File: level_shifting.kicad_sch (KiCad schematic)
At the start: 22 parts, among them J48 Conn_02x08_Odd_Even, J49 Conn_01x04, J50 Conn_02x08_Odd_Even, U25 TXS0108EPW

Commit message: WIP v0.2.0 changes
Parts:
- removed J48, J50: Conn_02x08_Odd_Even, HL_Connector_Pad_2.54mm:Pad_2x08_P2.54_1.7x1.7_Rect-Oct, symbol Connector_Generic:Conn_02x08_Odd_Even
- removed J49: Conn_01x04, HL_Connector_Pad_2.54mm:Pad_1x04_P2.54_1.7x1.7_Rect-Rnd-Rnd-Rect, symbol Connector_Generic:Conn_01x04
- added J106: Conn_01x04, HL_Connector_Pad_2.54mm:Pad_1x04_P2.54_1.7x1.7_Rect, symbol Connector_Generic:Conn_01x04
- added J80, J85: Conn_01x08, HL_Connector_Pad_2.54mm:Pad_1x08_P2.54_1.7x1.7_Oct, symbol Connector_Generic:Conn_01x08
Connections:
- net Ac1: now also J85.1 (Pin_1)
- net Ac2: now also J85.2 (Pin_2)
- net Ac3: now also J85.3 (Pin_3)
- net Ac4: now also J85.4 (Pin_4)
- net Ac5: now also J85.5 (Pin_5)
- net Ac6: now also J85.6 (Pin_6)
- net Ac7: now also J85.7 (Pin_7)
- net Ac8: now also J85.8 (Pin_8)
- net Bc1: now also J80.1 (Pin_1)
- net Bc2: now also J80.2 (Pin_2)
- net Bc3: now also J80.3 (Pin_3)
- net Bc4: now also J80.4 (Pin_4)
- net Bc5: now also J80.5 (Pin_5)
- net Bc6: now also J80.6 (Pin_6)
- net Bc7: now also J80.7 (Pin_7)
- net Bc8: now also J80.8 (Pin_8)
- net GND: now also J106.1 (Pin_1), J106.2 (Pin_2), J106.3 (Pin_3), J106.4 (Pin_4)
- net VCCA renamed +3.3V
- net VCCB renamed +5V

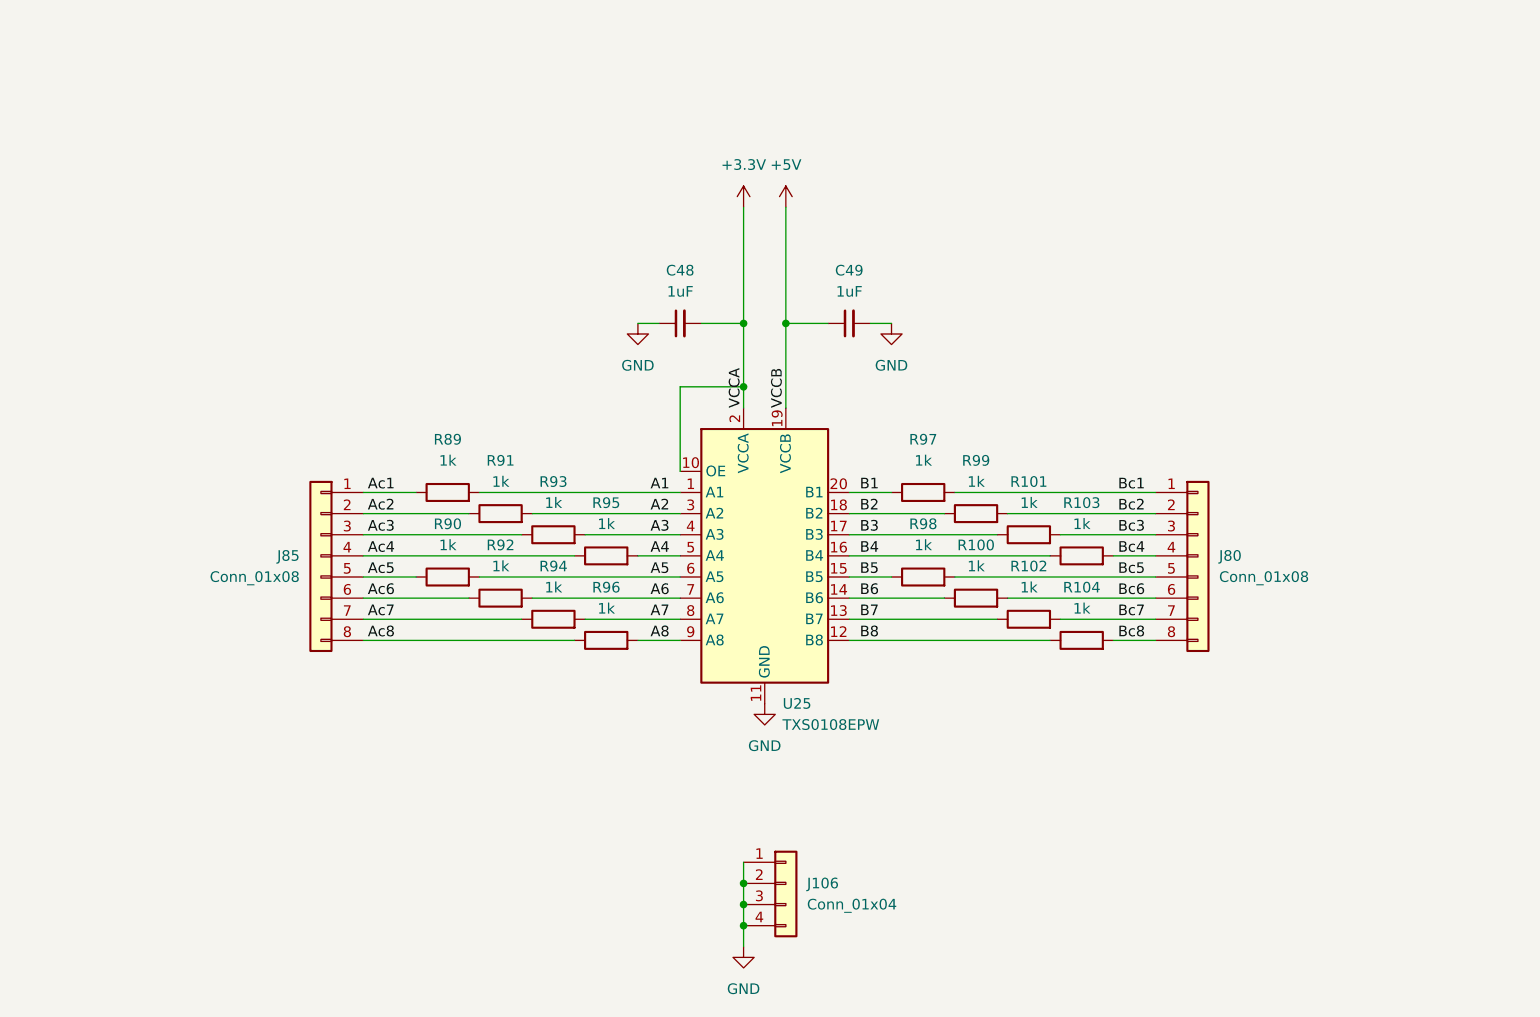
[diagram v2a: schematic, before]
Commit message: Assign part numbers and finish other 0.2.0 changes
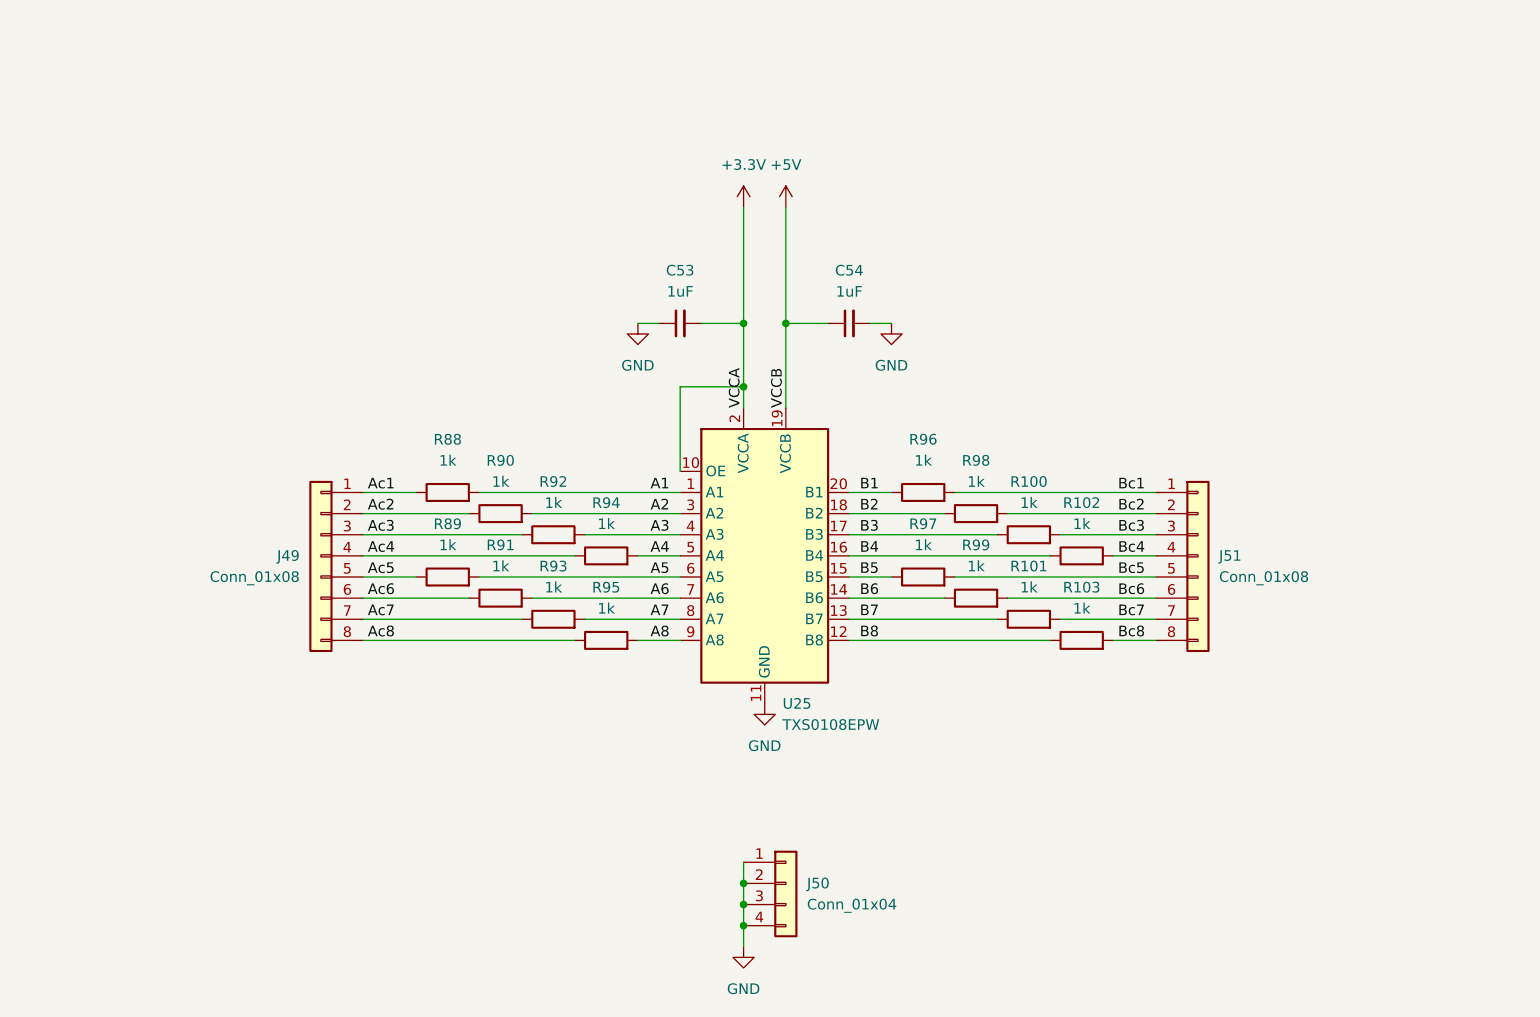
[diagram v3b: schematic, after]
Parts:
- J49: renamed from J85; LCSC (none) -> C492407
- J50: renamed from J106; LCSC (none) -> C2691448
- J51: renamed from J80; LCSC (none) -> C492407
- renumbered C48 to C53, C49 to C54, R101 to R100, R102 to R101, R103 to R102, R104 to R103, R89 to R88, R90 to R89, R91 to R90, R92 to R91, R93 to R92, R94 to R93, R95 to R94, R96 to R95, R97 to R96, R98 to R97, R99 to R98, R100 to R99
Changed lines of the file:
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@@
 		(dnp no)
 		(fields_autoplaced yes)
-		(property "Reference" "#PWR0280"
+		(property "Reference" "#PWR0205"
 			(at 135.89 46.99 0)
 			(effects
@@
 			(project "HALSPA"
 				(path "/7eeba806-440e-4671-bc07-69fe183910a7/47d24875-8df4-4f2a-9eb7-424cf9f25e0d"
-					(reference "#PWR0280")
+					(reference "#PWR0205")
 					(unit 1)
 				)
@@
 		(dnp no)
 		(fields_autoplaced yes)
-		(property "Reference" "C48"
+		(property "Reference" "C53"
 			(at 123.1963 50.8 90)
 			(effects
@@
 			(project ""
 				(path "/7eeba806-440e-4671-bc07-69fe183910a7/47d24875-8df4-4f2a-9eb7-424cf9f25e0d"
-					(reference "C48")
+					(reference "C53")
 					(unit 1)
 				)
@@
 		(dnp no)
 		(fields_autoplaced yes)
-		(property "Reference" "R95"
+		(property "Reference" "R94"
 			(at 114.3 78.74 90)
 			(effects
@@
 			(project "HALSPA"
 				(path "/7eeba806-440e-4671-bc07-69fe183910a7/47d24875-8df4-4f2a-9eb7-424cf9f25e0d"
-					(reference "R95")
+					(reference "R94")
 					(unit 1)
 				)
@@
 		(dnp no)
 		(fields_autoplaced yes)
-		(property "Reference" "C49"
+		(property "Reference" "C54"
 			(at 143.5163 50.8 90)
 			(effects
@@
 			(project "HALSPA"
 				(path "/7eeba806-440e-4671-bc07-69fe183910a7/47d24875-8df4-4f2a-9eb7-424cf9f25e0d"
-					(reference "C49")
+					(reference "C54")
 					(unit 1)
 				)
@@
 		(dnp no)
 		(fields_autoplaced yes)
-		(property "Reference" "R93"
+		(property "Reference" "R92"
 			(at 107.95 76.2 90)
 			(effects
@@
 			(project "HALSPA"
 				(path "/7eeba806-440e-4671-bc07-69fe183910a7/47d24875-8df4-4f2a-9eb7-424cf9f25e0d"
-					(reference "R93")
+					(reference "R92")
 					(unit 1)
 				)
@@
 		(dnp no)
 		(fields_autoplaced yes)
-		(property "Reference" "R92"
+		(property "Reference" "R91"
 			(at 101.6 83.82 90)
 			(effects
@@
 			(project "HALSPA"
 				(path "/7eeba806-440e-4671-bc07-69fe183910a7/47d24875-8df4-4f2a-9eb7-424cf9f25e0d"
-					(reference "R92")
+					(reference "R91")
 					(unit 1)
 				)
@@
 		(dnp no)
 		(fields_autoplaced yes)
-		(property "Reference" "R94"
+		(property "Reference" "R93"
 			(at 107.95 86.36 90)
 			(effects
@@
 			(project "HALSPA"
 				(path "/7eeba806-440e-4671-bc07-69fe183910a7/47d24875-8df4-4f2a-9eb7-424cf9f25e0d"
-					(reference "R94")
+					(reference "R93")
 					(unit 1)
 				)
@@
 		(dnp no)
 		(fields_autoplaced yes)
-		(property "Reference" "#PWR0194"
+		(property "Reference" "#PWR0206"
 			(at 148.59 63.5 0)
 			(effects
@@
 			(project "HALSPA"
 				(path "/7eeba806-440e-4671-bc07-69fe183910a7/47d24875-8df4-4f2a-9eb7-424cf9f25e0d"
-					(reference "#PWR0194")
+					(reference "#PWR0206")
 					(unit 1)
 				)
@@
 		(dnp no)
 		(fields_autoplaced yes)
-		(property "Reference" "R91"
+		(property "Reference" "R90"
 			(at 101.6 73.66 90)
 			(effects
@@
 			(project "HALSPA"
 				(path "/7eeba806-440e-4671-bc07-69fe183910a7/47d24875-8df4-4f2a-9eb7-424cf9f25e0d"
-					(reference "R91")
+					(reference "R90")
 					(unit 1)
 				)
@@
 		(dnp no)
 		(fields_autoplaced yes)
-		(property "Reference" "R104"
+		(property "Reference" "R103"
 			(at 171.45 88.9 90)
 			(effects
@@
 			(project "HALSPA"
 				(path "/7eeba806-440e-4671-bc07-69fe183910a7/47d24875-8df4-4f2a-9eb7-424cf9f25e0d"
-					(reference "R104")
+					(reference "R103")
 					(unit 1)
 				)
@@
 		(dnp no)
 		(fields_autoplaced yes)
-		(property "Reference" "R101"
+		(property "Reference" "R100"
 			(at 165.1 76.2 90)
 			(effects
@@
 			(project "HALSPA"
 				(path "/7eeba806-440e-4671-bc07-69fe183910a7/47d24875-8df4-4f2a-9eb7-424cf9f25e0d"
-					(reference "R101")
+					(reference "R100")
 					(unit 1)
 				)
@@
 		(dnp no)
 		(fields_autoplaced yes)
-		(property "Reference" "R90"
+		(property "Reference" "R89"
 			(at 95.25 81.28 90)
 			(effects
@@
 			(project "HALSPA"
 				(path "/7eeba806-440e-4671-bc07-69fe183910a7/47d24875-8df4-4f2a-9eb7-424cf9f25e0d"
-					(reference "R90")
+					(reference "R89")
 					(unit 1)
 				)
@@
 		(dnp no)
 		(fields_autoplaced yes)
-		(property "Reference" "R89"
+		(property "Reference" "R88"
 			(at 95.25 71.12 90)
 			(effects
@@
 			(project "HALSPA"
 				(path "/7eeba806-440e-4671-bc07-69fe183910a7/47d24875-8df4-4f2a-9eb7-424cf9f25e0d"
-					(reference "R89")
+					(reference "R88")
 					(unit 1)
 				)
@@
 		(dnp no)
 		(fields_autoplaced yes)
-		(property "Reference" "R99"
+		(property "Reference" "R98"
 			(at 158.75 73.66 90)
 			(effects
@@
 			(project "HALSPA"
 				(path "/7eeba806-440e-4671-bc07-69fe183910a7/47d24875-8df4-4f2a-9eb7-424cf9f25e0d"
-					(reference "R99")
+					(reference "R98")
 					(unit 1)
 				)
@@
 		(dnp no)
 		(fields_autoplaced yes)
-		(property "Reference" "R98"
+		(property "Reference" "R97"
 			(at 152.4 81.28 90)
 			(effects
@@
 			(project "HALSPA"
 				(path "/7eeba806-440e-4671-bc07-69fe183910a7/47d24875-8df4-4f2a-9eb7-424cf9f25e0d"
-					(reference "R98")
+					(reference "R97")
 					(unit 1)
 				)
@@
 		(dnp no)
 		(fields_autoplaced yes)
-		(property "Reference" "R103"
+		(property "Reference" "R102"
 			(at 171.45 78.74 90)
 			(effects
@@
 			(project "HALSPA"
 				(path "/7eeba806-440e-4671-bc07-69fe183910a7/47d24875-8df4-4f2a-9eb7-424cf9f25e0d"
-					(reference "R103")
+					(reference "R102")
 					(unit 1)
 				)
@@
 		(dnp no)
 		(fields_autoplaced yes)
-		(property "Reference" "R100"
+		(property "Reference" "R99"
 			(at 158.75 83.82 90)
 			(effects
@@
 			(project "HALSPA"
 				(path "/7eeba806-440e-4671-bc07-69fe183910a7/47d24875-8df4-4f2a-9eb7-424cf9f25e0d"
-					(reference "R100")
+					(reference "R99")
 					(unit 1)
 				)
@@
 		(dnp no)
 		(fields_autoplaced yes)
-		(property "Reference" "R97"
+		(property "Reference" "R96"
 			(at 152.4 71.12 90)
 			(effects
@@
 			(project "HALSPA"
 				(path "/7eeba806-440e-4671-bc07-69fe183910a7/47d24875-8df4-4f2a-9eb7-424cf9f25e0d"
-					(reference "R97")
+					(reference "R96")
 					(unit 1)
 				)
@@
 		(dnp no)
 		(fields_autoplaced yes)
-		(property "Reference" "R102"
+		(property "Reference" "R101"
 			(at 165.1 86.36 90)
 			(effects
@@
 			(project "HALSPA"
 				(path "/7eeba806-440e-4671-bc07-69fe183910a7/47d24875-8df4-4f2a-9eb7-424cf9f25e0d"
-					(reference "R102")
+					(reference "R101")
 					(unit 1)
 				)
@@
 		(dnp no)
 		(fields_autoplaced yes)
-		(property "Reference" "#PWR0191"
+		(property "Reference" "#PWR0201"
 			(at 118.11 63.5 0)
 			(effects
@@
 			(project ""
 				(path "/7eeba806-440e-4671-bc07-69fe183910a7/47d24875-8df4-4f2a-9eb7-424cf9f25e0d"
-					(reference "#PWR0191")
+					(reference "#PWR0201")
 					(unit 1)
 				)
@@
 		(dnp no)
 		(fields_autoplaced yes)
-		(property "Reference" "J80"
+		(property "Reference" "J51"
 			(at 187.96 85.0899 0)
 			(effects
@@
 			)
 		)
+		(property "LCSC" "C492407"
+			(at 185.42 85.09 0)
+			(effects
+				(font
+					(size 1.27 1.27)
+				)
+				(hide yes)
+			)
+		)
 		(pin "1"
 		)
@@
 			(project "HALSPA"
 				(path "/7eeba806-440e-4671-bc07-69fe183910a7/47d24875-8df4-4f2a-9eb7-424cf9f25e0d"
-					(reference "J80")
+					(reference "J51")
 					(unit 1)
 				)
@@
 		(dnp no)
 		(fields_autoplaced yes)
-		(property "Reference" "#PWR0277"
+		(property "Reference" "#PWR0202"
 			(at 130.81 46.99 0)
 			(effects
@@
 			(project ""
 				(path "/7eeba806-440e-4671-bc07-69fe183910a7/47d24875-8df4-4f2a-9eb7-424cf9f25e0d"
-					(reference "#PWR0277")
+					(reference "#PWR0202")
 					(unit 1)
 				)
@@
 		(dnp no)
 		(fields_autoplaced yes)
-		(property "Reference" "R96"
+		(property "Reference" "R95"
 			(at 114.3 88.9 90)
 			(effects
@@
 			(project "HALSPA"
 				(path "/7eeba806-440e-4671-bc07-69fe183910a7/47d24875-8df4-4f2a-9eb7-424cf9f25e0d"
-					(reference "R96")
+					(reference "R95")
 					(unit 1)
 				)
@@
 		(dnp no)
 		(fields_autoplaced yes)
-		(property "Reference" "#PWR0209"
+		(property "Reference" "#PWR0203"
 			(at 130.81 138.43 0)
 			(effects
@@
 			(project "HALSPA"
 				(path "/7eeba806-440e-4671-bc07-69fe183910a7/47d24875-8df4-4f2a-9eb7-424cf9f25e0d"
-					(reference "#PWR0209")
+					(reference "#PWR0203")
 					(unit 1)
 				)
@@
 		(on_board yes)
 		(dnp no)
-		(property "Reference" "J85"
+		(property "Reference" "J49"
 			(at 77.47 85.0899 0)
 			(effects
@@
 			)
 		)
+		(property "LCSC" "C492407"
+			(at 80.01 85.09 0)
+			(effects
+				(font
+					(size 1.27 1.27)
+				)
+				(hide yes)
+			)
+		)
 		(pin "1"
 		)
@@
 			(project "HALSPA"
 				(path "/7eeba806-440e-4671-bc07-69fe183910a7/47d24875-8df4-4f2a-9eb7-424cf9f25e0d"
-					(reference "J85")
+					(reference "J49")
 					(unit 1)
 				)
@@
 		(dnp no)
 		(fields_autoplaced yes)
-		(property "Reference" "J106"
+		(property "Reference" "J50"
 			(at 138.43 124.4599 0)
 			(effects
@@
 			)
 		)
+		(property "LCSC" "C2691448"
+			(at 135.89 124.46 0)
+			(effects
+				(font
+					(size 1.27 1.27)
+				)
+				(hide yes)
+			)
+		)
 		(pin "4"
 		)
@@
 			(project "HALSPA"
 				(path "/7eeba806-440e-4671-bc07-69fe183910a7/47d24875-8df4-4f2a-9eb7-424cf9f25e0d"
-					(reference "J106")
+					(reference "J50")
 					(unit 1)
 				)
@@
 		(dnp no)
 		(fields_autoplaced yes)
-		(property "Reference" "#PWR0193"
+		(property "Reference" "#PWR0204"
 			(at 133.35 109.22 0)
 			(effects
@@
 			(project "HALSPA"
 				(path "/7eeba806-440e-4671-bc07-69fe183910a7/47d24875-8df4-4f2a-9eb7-424cf9f25e0d"
-					(reference "#PWR0193")
-					(unit 1)
-				)
+					(reference "#PWR0204")
+					(unit 1)
+				)

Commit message: Update the title blocks
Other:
- company: (none) -> Hat Labs Oy
- title: (none) -> HALSPA - Hat Labs Spaghetti Board
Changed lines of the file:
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@@
 	(generator_version "9.0")
 	(paper "A4")
+	(title_block
+		(title "HALSPA - Hat Labs Spaghetti Board")
+		(date "2025-04-17")
+		(rev "v0.2.0")
+		(company "Hat Labs Oy")
+		(comment 1 "See the accompanying LICENSE.md file for license details.")
+	)
 	(junction
 		(at 130.81 127)

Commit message: Add JLCPCB corrections
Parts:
- J49, J51: JLCPCB_CORRECTION (none) -> 0;8.89;270
- J50: JLCPCB_CORRECTION (none) -> 0;3.81;270
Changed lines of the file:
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@@
+			)
+		)
+		(property "JLCPCB_CORRECTION" "0;8.89;270"
+			(at 185.42 85.09 0)
+			(effects
+				(font
+					(size 1.27 1.27)
+				)
+				(hide yes)
 			)
 		)
@@
 			)
 		)
+		(property "JLCPCB_CORRECTION" "0;8.89;270"
+			(at 80.01 85.09 0)
+			(effects
+				(font
+					(size 1.27 1.27)
+				)
+				(hide yes)
+			)
+		)
 		(pin "1"
 		)
@@
 			(at 135.89 124.46 0)
 			(effects
+				(font
+					(size 1.27 1.27)
+				)
+				(hide yes)
+			)
+		)
+		(property "JLCPCB_CORRECTION" "0;3.81;270"
+			(at 135.89 124.46 0)
+			(effects
